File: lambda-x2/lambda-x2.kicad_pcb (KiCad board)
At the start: 4 copper layers, 81.8 x 100.9 mm, 260 parts, among them J1 FTSH-107-01-F-DV-K, J3 Conn_02x02_Odd_Even, J4 Conn_01x10, P1 33311-24AW-2, Q1 BTS3028, Q2 BTS3028, Q3 BTS3028, Q4 BTS3028, U1 MAX31855KASA, U10 MCP6002T-I/SN, U11 GS8332-SR, U12 MCP6002T-I/SN, U13 MCP6002T-I/SN, U14 MAX31855KASA, U15 MAX31856, U16 MAX31856, U17 MCP6002T-I/SN, U18 JDY-33, U2 STM32F103C6Tx, U3 MCP6002T-I/SN, U4 LM78M05_TO252, U5 XC6206P332MR, U6 REF3033, U7 MCP6002T-I/SN, U8 TJA1051T-3, U9 GS8332-SR

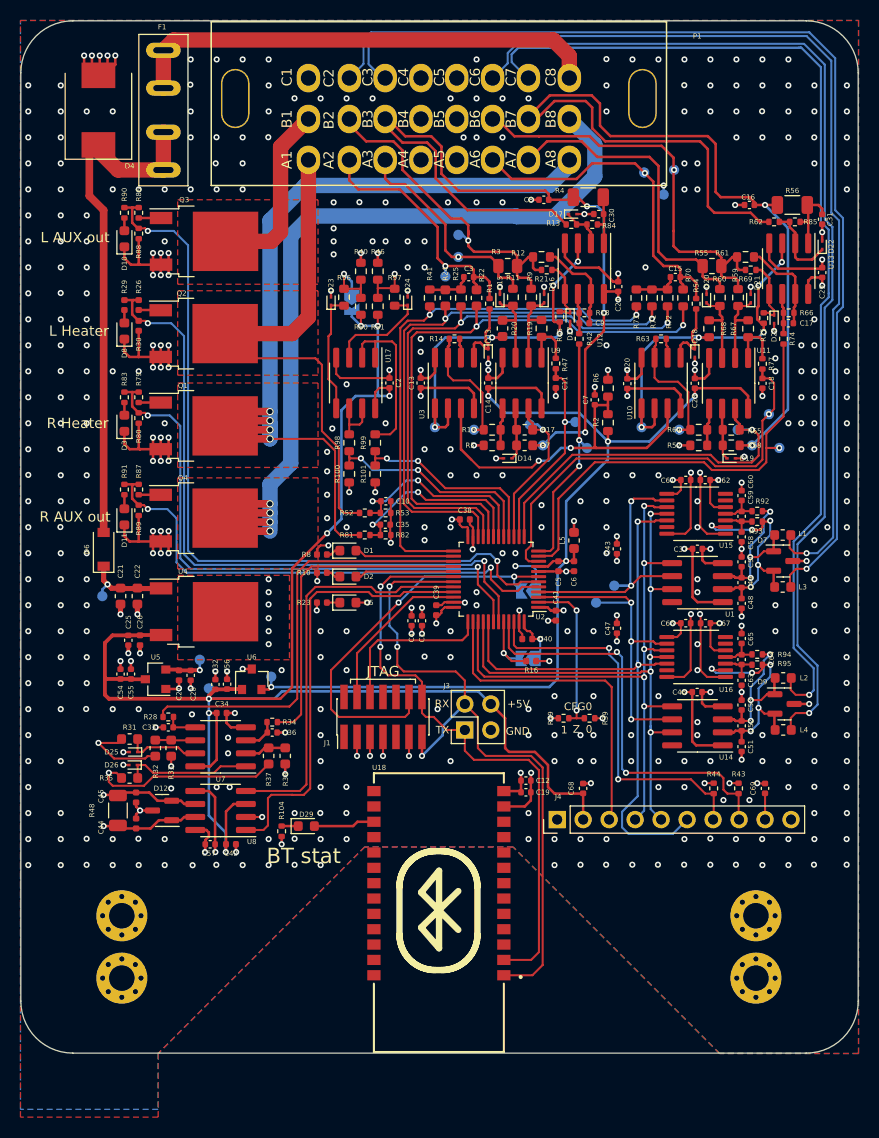
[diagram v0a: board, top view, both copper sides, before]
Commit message: lambda-x2: switch to 64-pin MCU
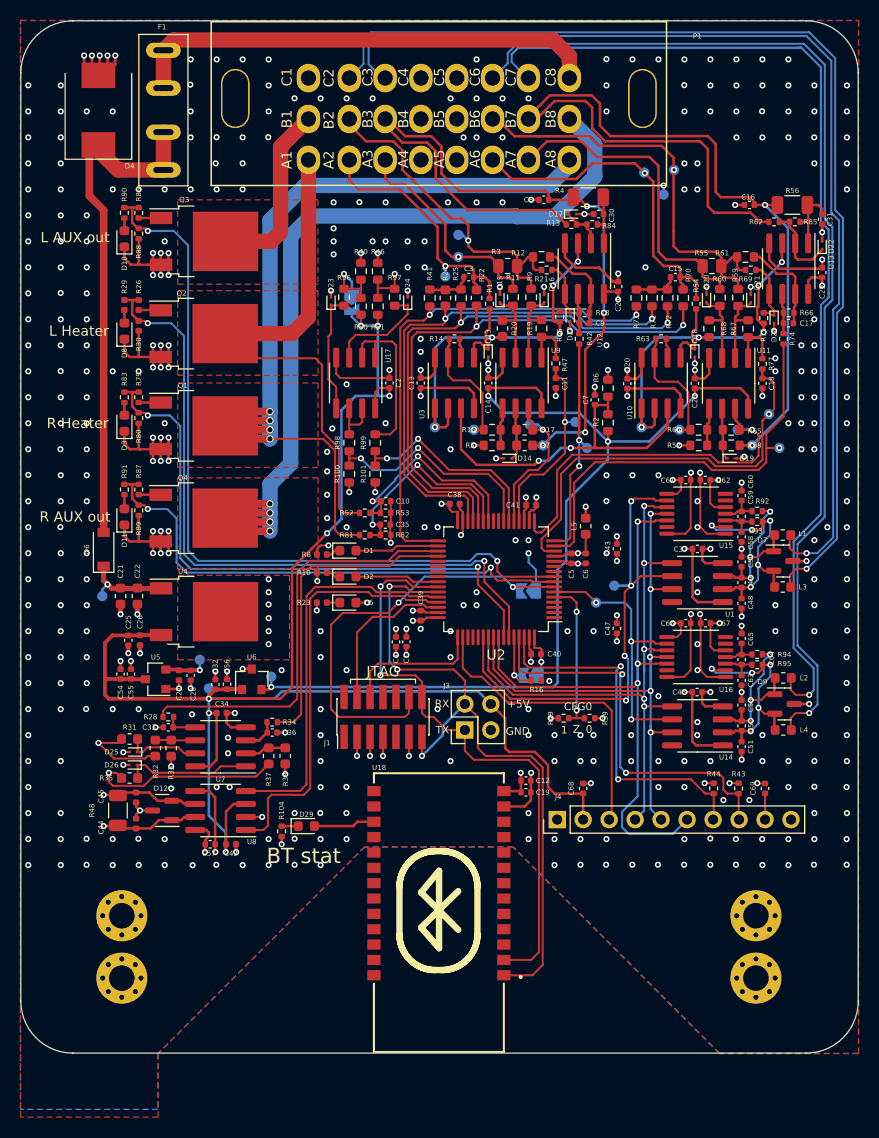
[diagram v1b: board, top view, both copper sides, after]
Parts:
- U2: footprint Package_QFP:LQFP-48_7x7mm_P0.5mm -> Package_QFP:LQFP-64_10x10mm_P0.5mm
- moved C41 11.1 mm to (142.5, 79.1), turned to 0 degrees
- moved C1 2.56 mm to (130.3, 92.5)
- moved C4 2.56 mm to (129.3, 92.5)
- moved R16 1.97 mm to (143.0, 96.3)
- moved C38 1.81 mm to (135.0, 79.0)
- moved L5 1.81 mm to (147.8, 81.2)
- moved C40 1.71 mm to (143.0, 93.7)
- moved JP3 1.68 mm to (142.5, 95.8)
- moved C39 1.61 mm to (131.7, 89.9)
- moved C5 1.48 mm to (146.4, 84.3)
- moved C6 1.37 mm to (147.8, 84.3)
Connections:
- U2 pad 1: +3V3 -> unconnected-(U2-Pad1)
- U2 pad 10: /R_Ip_sense -> unconnected-(U2-Pad10)
- U2 pad 11: /R_Ip_dac -> unconnected-(U2-Pad11)
- U2 pad 12: /L_Ip_dac -> GND
- U2 pad 13: /R_Un_3x_sense -> VDDA
- U2 pad 14: /L_Ip_sense -> /R_Ip_sense
- U2 pad 15: /L_Un_3x_sense -> /R_Ip_dac
- U2 pad 16: /R_AUX_ADC -> /L_Ip_dac
- U2 pad 17: /L_AUX_ADC -> /R_Un_3x_sense
- U2 pad 18: /L_Heater_sense -> GND
- U2 pad 19: /R_Heater_sense -> +3V3
- U2 pad 2: /config0 -> unconnected-(U2-Pad2)
- U2 pad 20: /Nernst_4.9_bias -> /L_Ip_sense
- U2 pad 21: /Nernst_ADV_esr_drive -> /L_Un_3x_sense
- U2 pad 22: /Nernst_4.9_esr_drive -> /R_AUX_ADC
- U2 pad 23: GND -> /L_AUX_ADC
- U2 pad 24: +3V3 -> unconnected-(U2-Pad24)
- U2 pad 25: /Nernst_4.2_esr_drive -> unconnected-(U2-Pad25)
- U2 pad 26: /LED_BLUE -> /L_Heater_sense
- U2 pad 27: /PWMout1 -> /R_Heater_sense
- U2 pad 28: /PWMout2 -> /Nernst_4.9_bias
- U2 pad 29: /LED_GREEN -> /Nernst_ADV_esr_drive
- U2 pad 3: /SPI1_CS1 -> unconnected-(U2-Pad3)
- U2 pad 30: /UART_TX -> /Nernst_4.9_esr_drive
- U2 pad 31: /UART_RX -> GND
- U2 pad 32: /CAN_RX -> +3V3
- U2 pad 33: /CAN_TX -> /Nernst_4.2_esr_drive
- U2 pad 34: /SWDIO -> /LED_BLUE
- U2 pad 35: GND -> /PWMout1
- U2 pad 36: +3V3 -> /PWMout2
- U2 pad 37: /SWCLK -> unconnected-(U2-Pad37)
- U2 pad 38: /SPI1_CS2 -> unconnected-(U2-Pad38)
- U2 pad 39: /SPI1_SCK -> unconnected-(U2-Pad39)
- U2 pad 4: /SPI1_CS0 -> unconnected-(U2-Pad4)
- U2 pad 40: /SPI1_MISO -> unconnected-(U2-Pad40)
- U2 pad 41: /SPI1_MOSI -> /LED_GREEN
- U2 pad 42: /R_heater_pwm -> /UART_TX
- U2 pad 43: /L_heater_pwm -> /UART_RX
- U2 pad 44: /Boot0 -> /CAN_RX
- U2 pad 45: /I2C1_SCL -> /CAN_TX
- U2 pad 46: /I2C1_SDA -> /SWDIO
- U2 pad 5: /R_OUT_en -> /config0
- U2 pad 6: /L_OUT_en -> /SPI1_CS1
- U2 pad 8: GND -> /R_OUT_en
- U2 pad 9: VDDA -> /L_OUT_en
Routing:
- net /SPI1_CS0: track 29.1 -> 50.0 mm, vias 2 -> 4
- net /SPI1_CS1: track 31.7 -> 26.6 mm
- net /nRESET: track 39.2 -> 43.1 mm
- net /Nernst_4.9_bias: track 58.2 -> 54.7 mm
- net /Nernst_ADV_esr_drive: track 56.5 -> 53.3 mm
- net /Nernst_4.9_esr_drive: track 55.0 -> 51.9 mm
- net /Nernst_4.2_esr_drive: track 53.0 -> 50.5 mm
- net /SWCLK: track 16.1 -> 13.7 mm
- net /I2C1_SCL: track 40.7 -> 38.4 mm
- net /SPI1_CS2: track 32.2 -> 30.1 mm
- net /L_heater_pwm: track 66.6 -> 68.5 mm
- net /R_heater_pwm: track 56.8 -> 58.8 mm
- net /SPI1_SCK: track 64.6 -> 62.9 mm
- net /R_Ip_sense: track 42.1 -> 40.5 mm
- net /L_Ip_dac: track 23.6 -> 22.1 mm
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
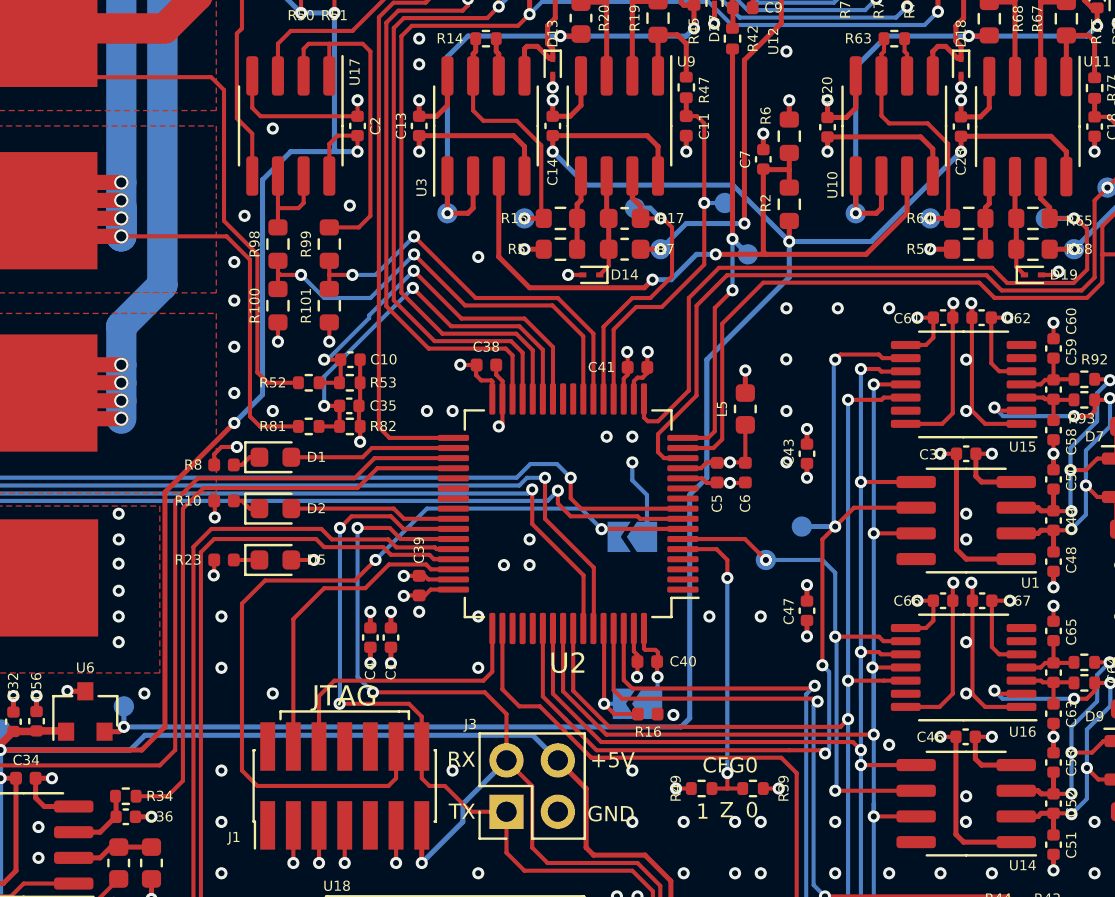
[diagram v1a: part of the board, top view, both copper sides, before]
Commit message: lambda-x2: add HSE, move pump to DAC outputs
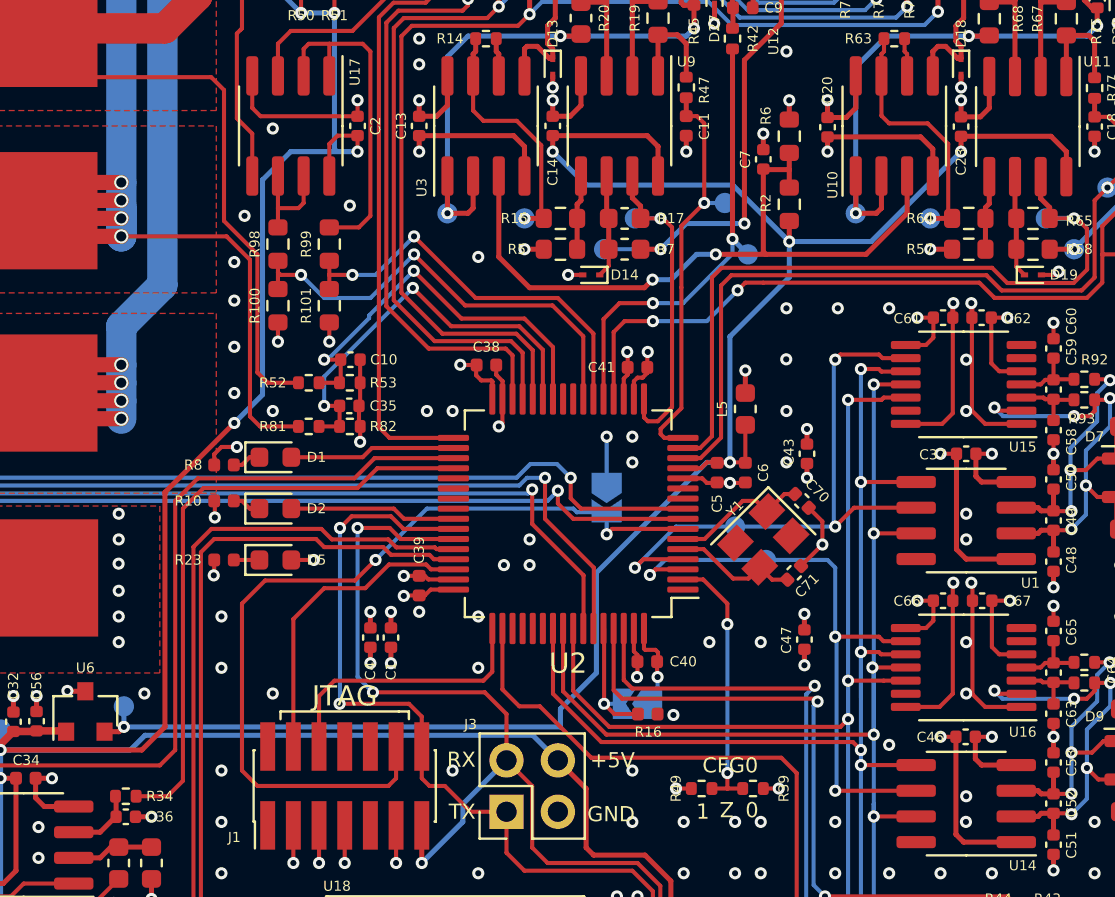
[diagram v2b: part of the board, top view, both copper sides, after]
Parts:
- added C70: 20pF 50V, Capacitor_SMD:C_0402_1005Metric, F.Cu at (150.6, 85.7)
- added C71: 20pF 50V, Capacitor_SMD:C_0402_1005Metric, F.Cu at (150.2, 89.3)
- added Y1: XXDCELNANF-8MHZ, Crystal:Crystal_SMD_3225-4Pin_3.2x2.5mm, F.Cu at (148.7, 87.6)
- moved TP25 3.30 mm to (147.3, 87.0)
- moved TP12 2.79 mm to (140.8, 73.3)
- moved JP2 2.32 mm to (141.0, 85.6), turned to -90 degrees
- moved C47 1.43 mm to (150.7, 92.6)
- moved TP5 0.51 mm to (142.4, 71.8)
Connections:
- U2 pad 15: /R_Ip_dac -> /R_Un_3x_sense
- U2 pad 16: /L_Ip_dac -> /L_Ip_sense
- U2 pad 17: /R_Un_3x_sense -> /L_Un_3x_sense
- U2 pad 2: unconnected-(U2-Pad2) -> /config0
- U2 pad 20: /L_Ip_sense -> /R_Ip_dac
- U2 pad 21: /L_Un_3x_sense -> /L_Ip_dac
- U2 pad 3: unconnected-(U2-Pad3) -> /SPI1_CS1
- U2 pad 4: unconnected-(U2-Pad4) -> /SPI1_CS0
- U2 pad 5: /config0 -> Net-(U2-Pad5)
- U2 pad 54: /SPI1_CS0 -> unconnected-(U2-Pad54)
- U2 pad 6: /SPI1_CS1 -> Net-(U2-Pad6)
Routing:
- net /SPI1_CS0: track 50.0 -> 29.8 mm, vias 4 -> 3
- net Net-(U2-Pad6): track 0.00 -> 6.90 mm
- net Net-(U2-Pad5): track 0.00 -> 6.25 mm
- net VDDA: track 102.2 -> 98.2 mm
- net /SPI1_CS1: track 26.6 -> 30.0 mm
- net /L_LSU_Vm: track 79.1 -> 81.8 mm
- net GND: track 275.7 -> 277.6 mm, vias 465 -> 466
- net /config0: track 15.2 -> 13.4 mm
- net /L_Ip_sense: track 19.2 -> 20.4 mm
- net /R_Ip_dac: track 41.6 -> 42.6 mm, vias 1 -> 3
- net /L_Un_3x_sense: track 15.9 -> 16.8 mm
- net /R_Ip_sense: track 40.5 -> 39.6 mm
- net /L_Ip_dac: track 22.1 -> 22.9 mm
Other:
- board text added: "RusEFI Lambda X2 Rev 1 https://rusefi.com/ By Dron_Gus https://github.com/dron0gus/"
- board text removed: "RusEFI Lambda X2 Rev 0 https://rusefi.com/ By Dron_Gus https://github.com/dron0gus/"

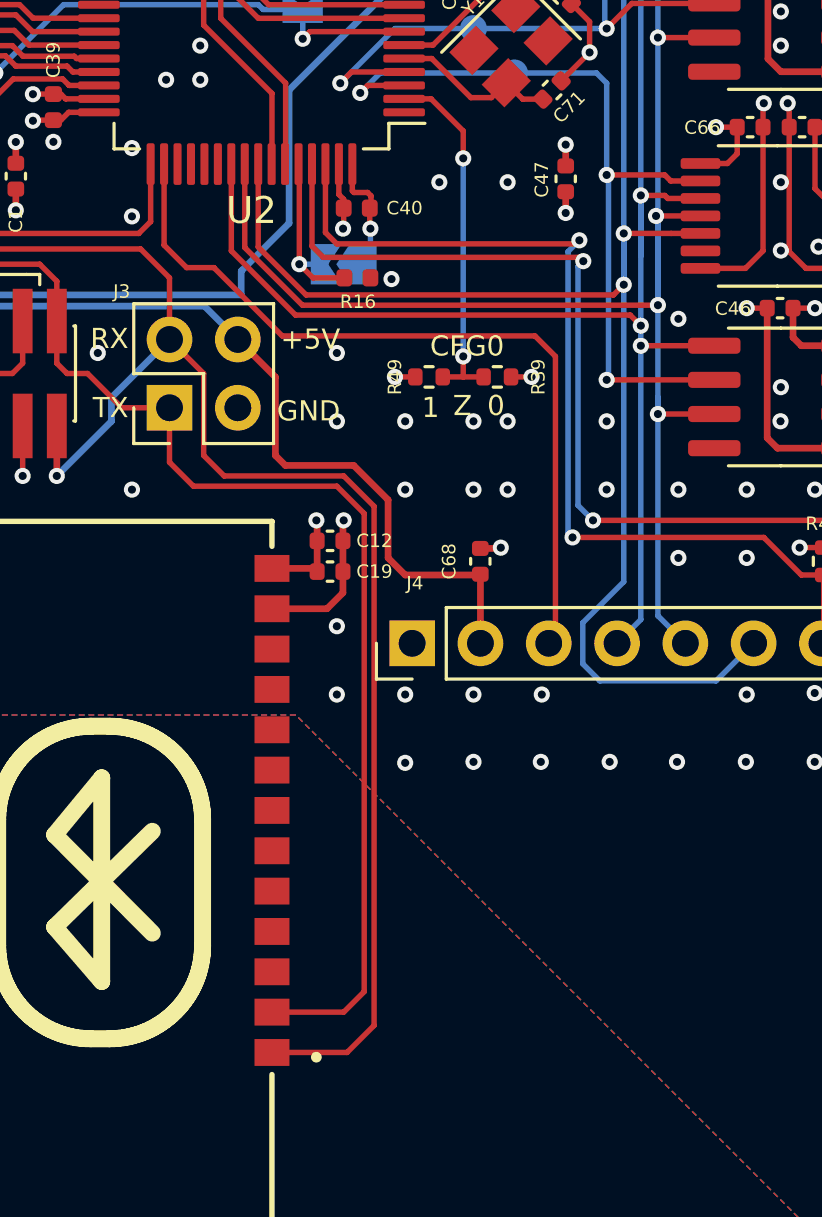
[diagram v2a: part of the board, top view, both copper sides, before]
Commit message: lambda-x2: move BT to UART4/USART3
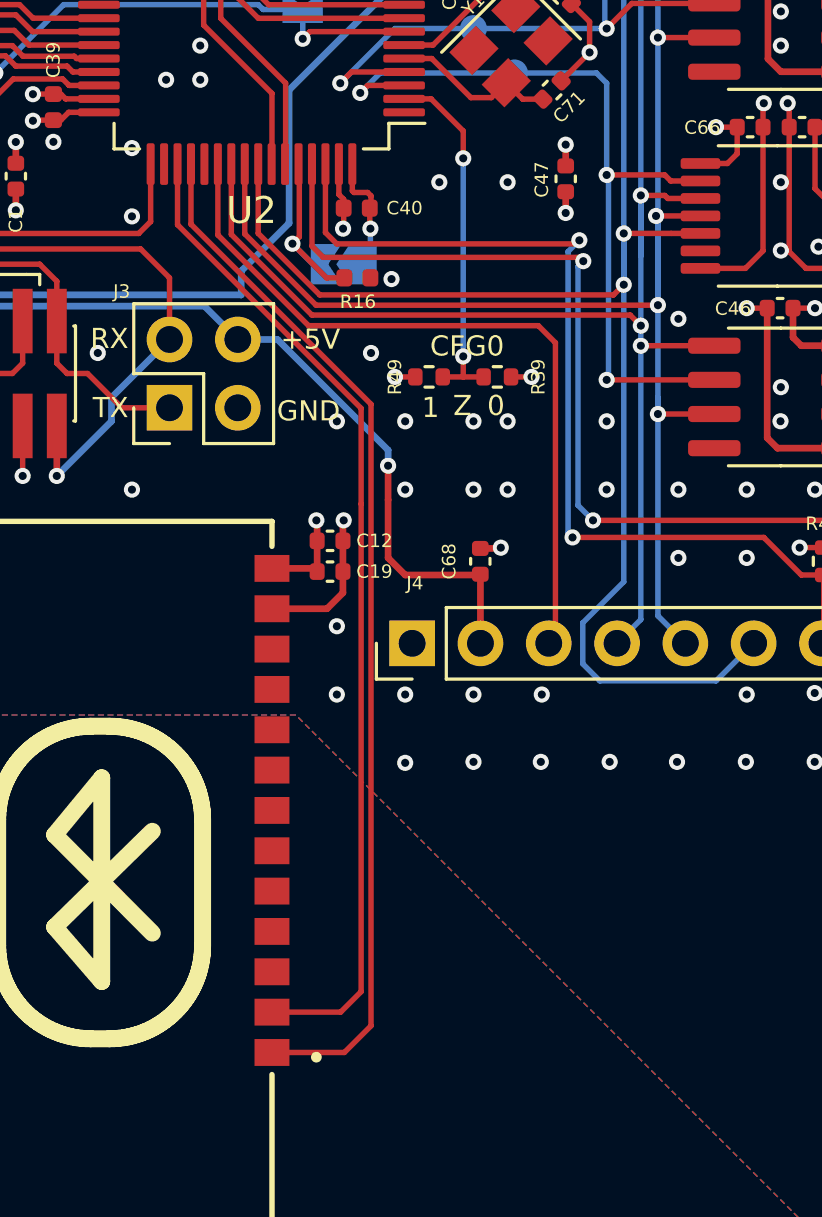
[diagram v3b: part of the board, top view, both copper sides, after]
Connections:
- U18 pad 1: /UART_RX -> /BT_UART_RX
- U18 pad 2: /UART_TX -> /BT_UART_TX
- U2 pad 50: /SPI1_CS2 -> unconnected-(U2-Pad50)
- U2 pad 51: unconnected-(U2-Pad51) -> /BT_UART_TX
- U2 pad 52: unconnected-(U2-Pad52) -> /BT_UART_RX
- U2 pad 54: unconnected-(U2-Pad54) -> /SPI1_CS2
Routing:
- net /BT_UART_RX: track 0.00 -> 38.9 mm
- net /BT_UART_TX: track 0.00 -> 37.2 mm
- net /UART_RX: track 66.9 -> 31.4 mm
- net /UART_TX: track 58.6 -> 27.1 mm
- net /SPI1_CS2: track 30.1 -> 28.1 mm
- net +5V: track 165.9 -> 165.3 mm, vias 7 -> 8
